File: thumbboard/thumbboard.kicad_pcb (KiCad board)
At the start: 2 copper layers, 63 x 36 mm, 8 parts, among them J1 Conn_01x05_MountingPin, SW1 SW_Push, SW2 SW_Push, SW3 SW_Push, SW4 SW_Push

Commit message: various tweaks, about to start on the carapace
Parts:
- added T1: Tab, PCM_kikit:Tab, F.Cu at (118.0, 77.2)
- added T2: Tab, PCM_kikit:Tab, F.Cu at (110.2, 85.0)
- added T3: Tab, PCM_kikit:Tab, F.Cu at (145.0, 77.2)
- added T4: Tab, PCM_kikit:Tab, F.Cu at (172.0, 77.2)
- added T5: Tab, PCM_kikit:Tab, F.Cu at (179.8, 85.0)
- added T6: Tab, PCM_kikit:Tab, F.Cu at (145.0, 115.2)
- J1: footprint Connector_FFC-FPC:TE_84952-5_1x05-1MP_P1.0mm_Horizontal -> panelization:FFC clamp fit 1x05 1.00mm
- moved REF** 3.00 mm to (127.0, 85.0)
- moved REF** 3.00 mm to (163.0, 85.0)
- moved SW1 3.00 mm to (118.0, 85.0)
- moved SW4 3.00 mm to (172.0, 85.0)
- moved SW3 2.00 mm to (145.0, 107.5)
- moved REF** 1.00 mm to (145.0, 96.0)
- moved J1 0.20 mm to (145.0, 80.0), turned to 180 degrees
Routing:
- net COL: track 104.6 -> 110.4 mm
- net ROW_C: track 20.9 -> 25.4 mm
- net ROW_D: track 42.0 -> 45.5 mm
- net ROW_A: track 32.3 -> 35.6 mm
- net ROW_B: track 8.46 -> 10.5 mm
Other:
- board size 63 x 36 mm -> 69 x 37.5 mm

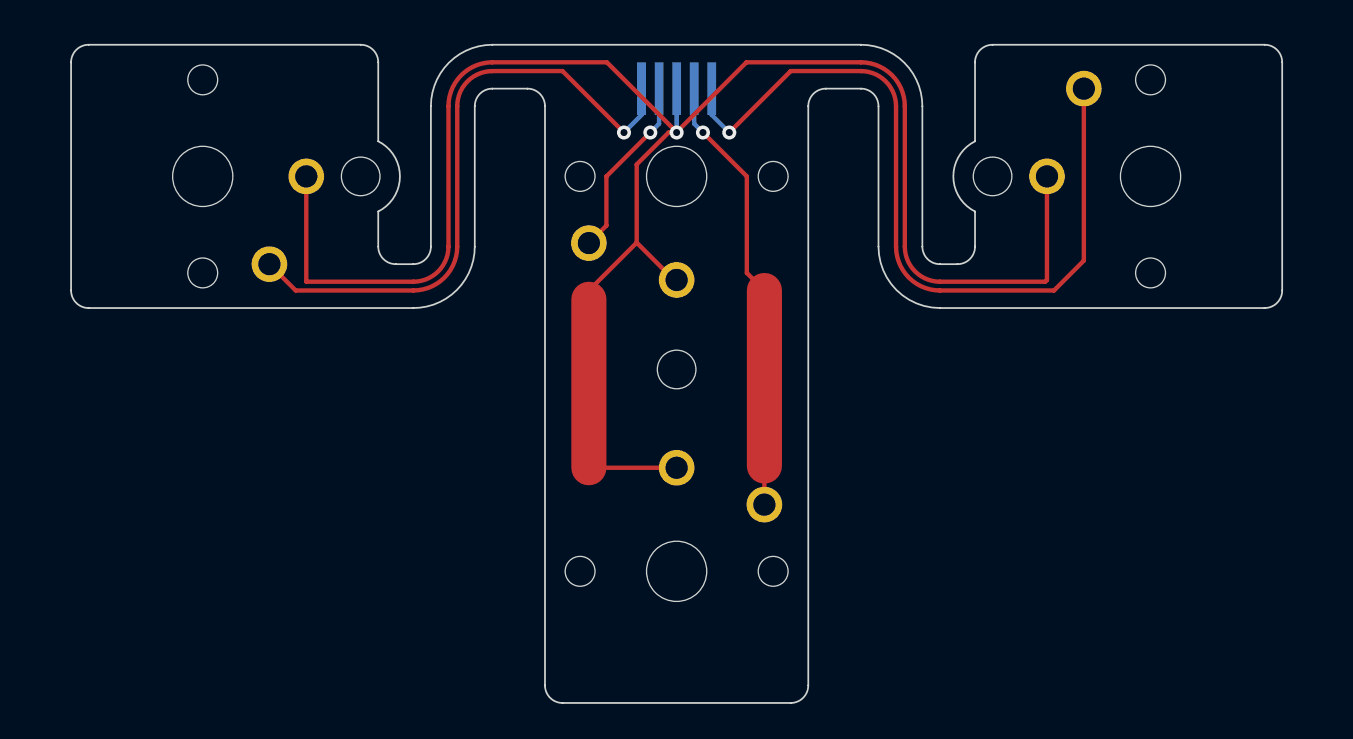
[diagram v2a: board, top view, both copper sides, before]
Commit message: create thumb cluster scaffold, tweak tc distances and shape
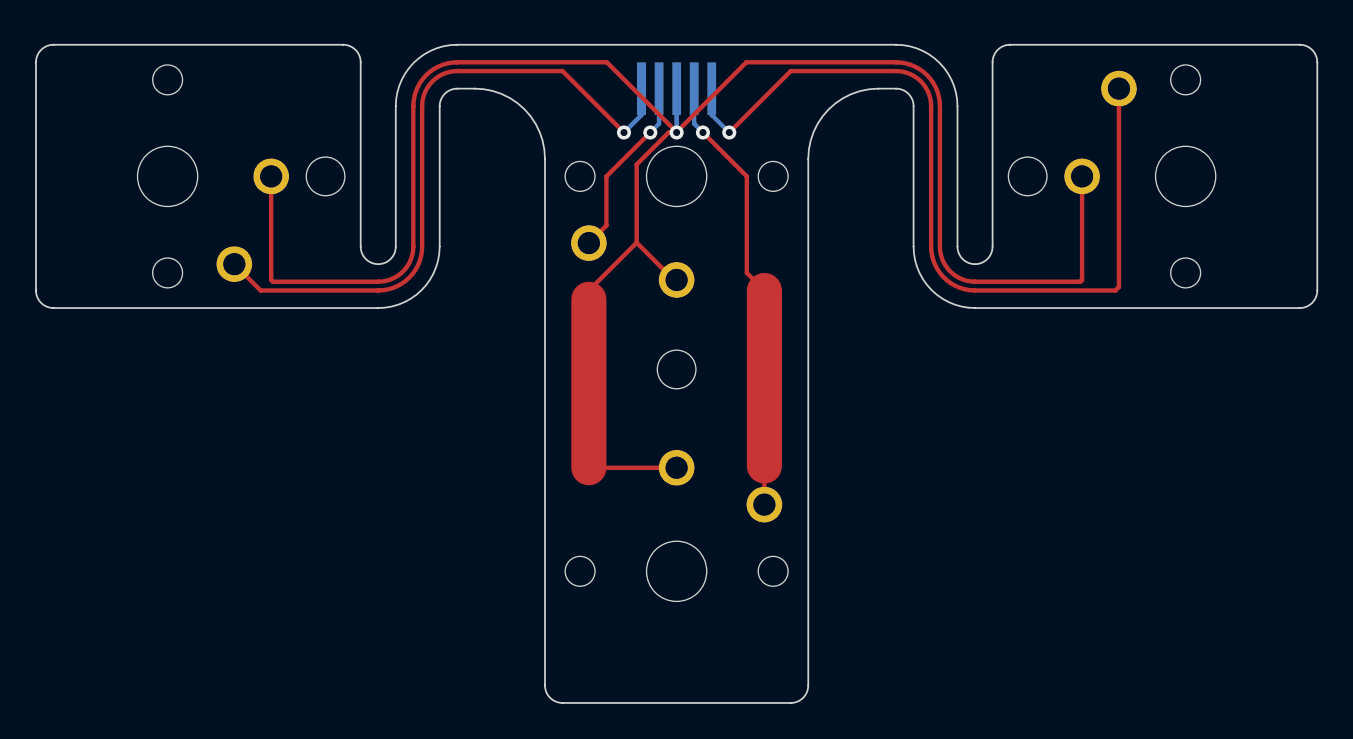
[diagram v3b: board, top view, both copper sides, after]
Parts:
- removed T1, T2: Tab, PCM_kikit:Tab
- added T4: Tab, PCM_kikit:Tab, F.Cu at (118.0, 77.2)
- added T5: Tab, PCM_kikit:Tab, F.Cu at (108.2, 85.0)
- REF**: moved to B.Cu
- moved REF** 2.00 mm to (125.0, 85.0), turned to 180 degrees
- moved REF** 2.00 mm to (165.0, 85.0)
- moved SW1 2.00 mm to (116.0, 85.0)
- moved SW4 2.00 mm to (174.0, 85.0)
- moved T5 2.00 mm to (181.8, 85.0)
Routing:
- net COL: track 110.4 -> 114.3 mm
- net ROW_D: track 45.5 -> 48.3 mm
- net ROW_A: track 35.6 -> 37.6 mm
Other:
- board size 69 x 37.5 mm -> 73 x 37.5 mm
